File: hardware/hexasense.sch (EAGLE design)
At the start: 15 parts, among them IC1 AT45DB161D-SU

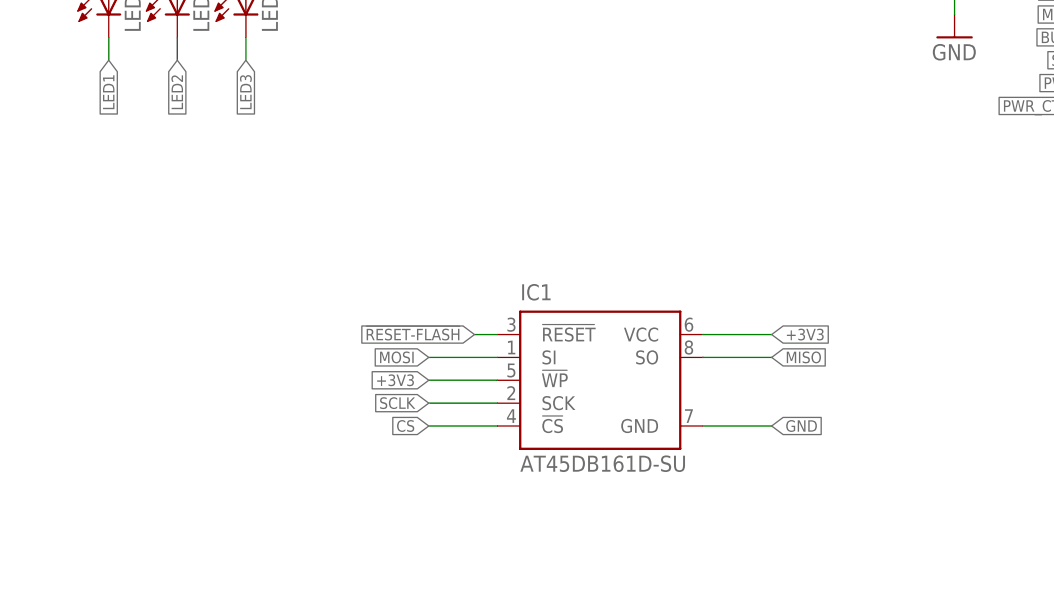
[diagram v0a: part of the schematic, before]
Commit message: added testpads to schematic
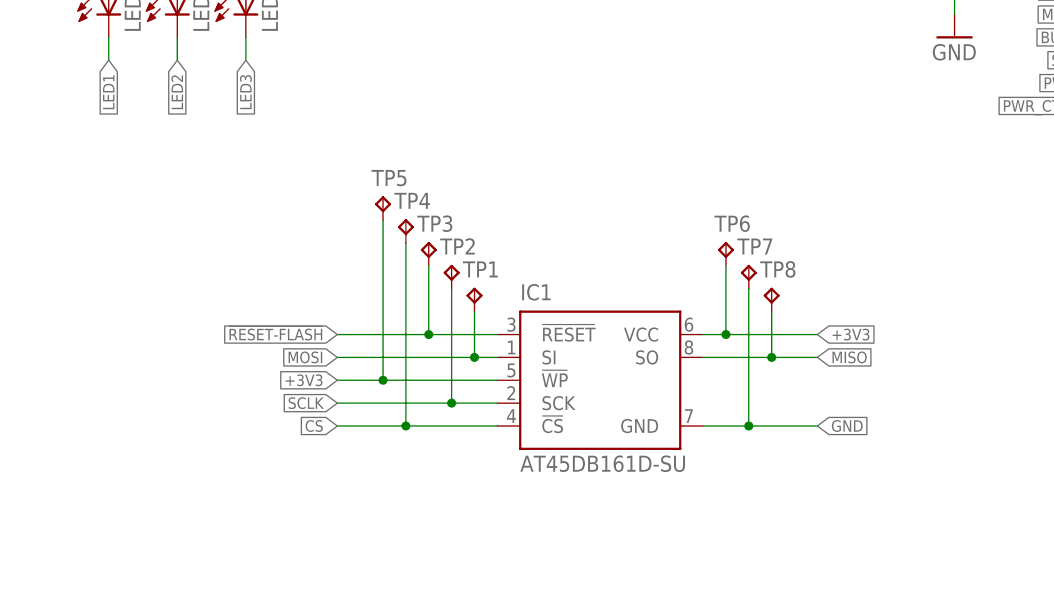
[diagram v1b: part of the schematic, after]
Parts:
- added TP1, TP2, TP3, TP4, TP5, TP6, TP7, TP8: TPB1,27, testpad:TPB1,27
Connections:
- net !RESET-FLASH: now also TP3.TP
- net +3V3: now also TP5.TP, TP6.TP
- net CS: now also TP4.TP
- net GND: now also TP7.TP
- net MISO: now also TP8.TP
- net MOSI: now also TP1.TP
- net SCLK: now also TP2.TP
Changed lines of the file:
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@@
 <part name="+3V6" library="supply1" deviceset="+3V3" device=""/>
 <part name="U$2" library="epaper" deviceset="EPAPER" device=""/>
+<part name="TP1" library="testpad" deviceset="TP" device="B1,27"/>
+<part name="TP2" library="testpad" deviceset="TP" device="B1,27"/>
+<part name="TP3" library="testpad" deviceset="TP" device="B1,27"/>
+<part name="TP4" library="testpad" deviceset="TP" device="B1,27"/>
+<part name="TP5" library="testpad" deviceset="TP" device="B1,27"/>
+<part name="TP6" library="testpad" deviceset="TP" device="B1,27"/>
+<part name="TP7" library="testpad" deviceset="TP" device="B1,27"/>
+<part name="TP8" library="testpad" deviceset="TP" device="B1,27"/>
 </parts>
 <sheets>
@@
 <instance part="+3V6" gate="G$1" x="99.06" y="167.64"/>
 <instance part="U$2" gate="G$1" x="213.36" y="144.78"/>
+<instance part="TP1" gate="G$1" x="124.46" y="114.3"/>
+<instance part="TP2" gate="G$1" x="121.92" y="116.84"/>
+<instance part="TP3" gate="G$1" x="119.38" y="119.38"/>
+<instance part="TP4" gate="G$1" x="116.84" y="121.92"/>
+<instance part="TP5" gate="G$1" x="114.3" y="124.46"/>
+<instance part="TP6" gate="G$1" x="152.4" y="119.38"/>
+<instance part="TP7" gate="G$1" x="154.94" y="116.84"/>
+<instance part="TP8" gate="G$1" x="157.48" y="114.3"/>
 </instances>
 <busses>
@@
 <segment>
 <pinref part="IC1" gate="G$1" pin="GND"/>
-<wire x1="149.86" y1="99.06" x2="157.48" y2="99.06" width="0.1524" layer="91"/>
-<label x="157.48" y="99.06" size="1.27" layer="95" xref="yes"/>
+<wire x1="149.86" y1="99.06" x2="154.94" y2="99.06" width="0.1524" layer="91"/>
+<label x="162.56" y="99.06" size="1.27" layer="95" xref="yes"/>
+<pinref part="TP7" gate="G$1" pin="TP"/>
+<wire x1="154.94" y1="99.06" x2="162.56" y2="99.06" width="0.1524" layer="91"/>
+<wire x1="154.94" y1="114.3" x2="154.94" y2="99.06" width="0.1524" layer="91"/>
+<junction x="154.94" y="99.06"/>
 </segment>
 <segment>
@@
 <segment>
 <pinref part="IC1" gate="G$1" pin="VCC"/>
-<wire x1="149.86" y1="109.22" x2="157.48" y2="109.22" width="0.1524" layer="91"/>
-<label x="157.48" y="109.22" size="1.27" layer="95" xref="yes"/>
+<wire x1="149.86" y1="109.22" x2="152.4" y2="109.22" width="0.1524" layer="91"/>
+<label x="162.56" y="109.22" size="1.27" layer="95" xref="yes"/>
+<pinref part="TP6" gate="G$1" pin="TP"/>
+<wire x1="152.4" y1="109.22" x2="162.56" y2="109.22" width="0.1524" layer="91"/>
+<wire x1="152.4" y1="116.84" x2="152.4" y2="109.22" width="0.1524" layer="91"/>
+<junction x="152.4" y="109.22"/>
 </segment>
 <segment>
 <pinref part="IC1" gate="G$1" pin="!WP"/>
-<wire x1="127" y1="104.14" x2="119.38" y2="104.14" width="0.1524" layer="91"/>
-<label x="119.38" y="104.14" size="1.27" layer="95" rot="R180" xref="yes"/>
+<wire x1="127" y1="104.14" x2="114.3" y2="104.14" width="0.1524" layer="91"/>
+<label x="109.22" y="104.14" size="1.27" layer="95" rot="R180" xref="yes"/>
+<pinref part="TP5" gate="G$1" pin="TP"/>
+<wire x1="114.3" y1="104.14" x2="109.22" y2="104.14" width="0.1524" layer="91"/>
+<wire x1="114.3" y1="121.92" x2="114.3" y2="104.14" width="0.1524" layer="91"/>
+<junction x="114.3" y="104.14"/>
 </segment>
 <segment>
@@
 <pinref part="IC1" gate="G$1" pin="SO"/>
 <wire x1="149.86" y1="106.68" x2="157.48" y2="106.68" width="0.1524" layer="91"/>
-<label x="157.48" y="106.68" size="1.27" layer="95" xref="yes"/>
+<label x="162.56" y="106.68" size="1.27" layer="95" xref="yes"/>
+<pinref part="TP8" gate="G$1" pin="TP"/>
+<wire x1="157.48" y1="106.68" x2="162.56" y2="106.68" width="0.1524" layer="91"/>
+<wire x1="157.48" y1="111.76" x2="157.48" y2="106.68" width="0.1524" layer="91"/>
+<junction x="157.48" y="106.68"/>
 </segment>
 <segment>
@@
 <segment>
 <pinref part="IC1" gate="G$1" pin="SI"/>
-<wire x1="127" y1="106.68" x2="119.38" y2="106.68" width="0.1524" layer="91"/>
-<label x="119.38" y="106.68" size="1.27" layer="95" rot="R180" xref="yes"/>
+<wire x1="127" y1="106.68" x2="124.46" y2="106.68" width="0.1524" layer="91"/>
+<label x="109.22" y="106.68" size="1.27" layer="95" rot="R180" xref="yes"/>
+<pinref part="TP1" gate="G$1" pin="TP"/>
+<wire x1="124.46" y1="106.68" x2="109.22" y2="106.68" width="0.1524" layer="91"/>
+<wire x1="124.46" y1="111.76" x2="124.46" y2="106.68" width="0.1524" layer="91"/>
+<junction x="124.46" y="106.68"/>
 </segment>
 <segment>
@@
 <segment>
 <pinref part="IC1" gate="G$1" pin="!CS"/>
-<wire x1="127" y1="99.06" x2="119.38" y2="99.06" width="0.1524" layer="91"/>
-<label x="119.38" y="99.06" size="1.27" layer="95" rot="R180" xref="yes"/>
+<wire x1="127" y1="99.06" x2="116.84" y2="99.06" width="0.1524" layer="91"/>
+<label x="109.22" y="99.06" size="1.27" layer="95" rot="R180" xref="yes"/>
+<pinref part="TP4" gate="G$1" pin="TP"/>
+<wire x1="116.84" y1="99.06" x2="109.22" y2="99.06" width="0.1524" layer="91"/>
+<wire x1="116.84" y1="119.38" x2="116.84" y2="99.06" width="0.1524" layer="91"/>
+<junction x="116.84" y="99.06"/>
 </segment>
 <segment>
@@
 <segment>
 <pinref part="IC1" gate="G$1" pin="!RESET"/>
-<wire x1="127" y1="109.22" x2="124.46" y2="109.22" width="0.1524" layer="91"/>
-<label x="124.46" y="109.22" size="1.27" layer="95" rot="R180" xref="yes"/>
+<wire x1="127" y1="109.22" x2="119.38" y2="109.22" width="0.1524" layer="91"/>
+<label x="109.22" y="109.22" size="1.27" layer="95" rot="R180" xref="yes"/>
+<pinref part="TP3" gate="G$1" pin="TP"/>
+<wire x1="119.38" y1="109.22" x2="109.22" y2="109.22" width="0.1524" layer="91"/>
+<wire x1="119.38" y1="116.84" x2="119.38" y2="109.22" width="0.1524" layer="91"/>
+<junction x="119.38" y="109.22"/>
 </segment>
 <segment>
@@
 <segment>
 <pinref part="IC1" gate="G$1" pin="SCK"/>
-<wire x1="127" y1="101.6" x2="119.38" y2="101.6" width="0.1524" layer="91"/>
-<label x="119.38" y="101.6" size="1.27" layer="95" rot="R180" xref="yes"/>
-</segment>
-</net>
+<wire x1="127" y1="101.6" x2="121.92" y2="101.6" width="0.1524" layer="91"/>
+<label x="109.22" y="101.6" size="1.27" layer="95" rot="R180" xref="yes"/>
+<pinref part="TP2" gate="G$1" pin="TP"/>
+<wire x1="121.92" y1="101.6" x2="109.22" y2="101.6" width="0.1524" layer="91"/>
+<wire x1="121.92" y1="114.3" x2="121.92" y2="101.6" width="0.1524" layer="91"/>
+<junction x="121.92" y="101.6"/>
+</segment>
+</net>

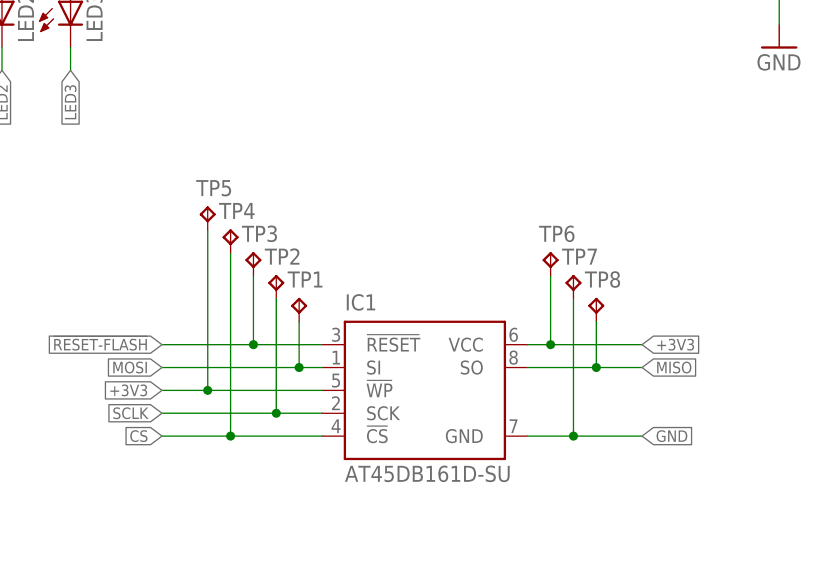
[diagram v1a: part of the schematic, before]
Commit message: testpads and placement print
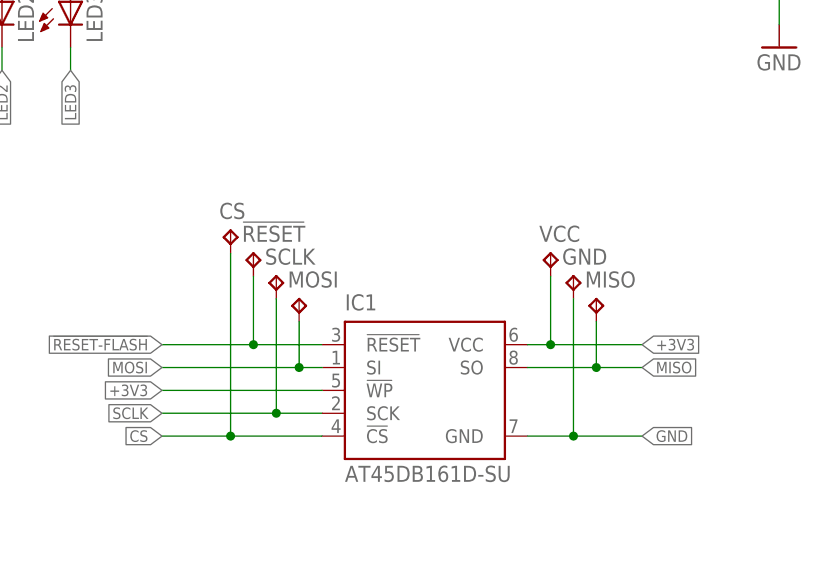
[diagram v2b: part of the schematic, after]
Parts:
- removed TP5: TPB1,27, testpad:TPB1,27
- renumbered TP1 to MOSI, TP2 to SCLK, TP3 to !RESET, TP4 to CS, TP6 to VCC, TP7 to GND, TP8 to MISO
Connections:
- net +3V3: no longer TP5.TP
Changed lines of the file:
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@@
 <part name="+3V6" library="supply1" deviceset="+3V3" device=""/>
 <part name="U$2" library="epaper" deviceset="EPAPER" device=""/>
-<part name="TP1" library="testpad" deviceset="TP" device="B1,27"/>
-<part name="TP2" library="testpad" deviceset="TP" device="B1,27"/>
-<part name="TP3" library="testpad" deviceset="TP" device="B1,27"/>
-<part name="TP4" library="testpad" deviceset="TP" device="B1,27"/>
-<part name="TP5" library="testpad" deviceset="TP" device="B1,27"/>
-<part name="TP6" library="testpad" deviceset="TP" device="B1,27"/>
-<part name="TP7" library="testpad" deviceset="TP" device="B1,27"/>
-<part name="TP8" library="testpad" deviceset="TP" device="B1,27"/>
+<part name="MOSI" library="testpad" deviceset="TP" device="B1,27"/>
+<part name="SCLK" library="testpad" deviceset="TP" device="B1,27"/>
+<part name="!RESET" library="testpad" deviceset="TP" device="B1,27"/>
+<part name="CS" library="testpad" deviceset="TP" device="B1,27"/>
+<part name="VCC" library="testpad" deviceset="TP" device="B1,27"/>
+<part name="GND" library="testpad" deviceset="TP" device="B1,27"/>
+<part name="MISO" library="testpad" deviceset="TP" device="B1,27"/>
 </parts>
 <sheets>
@@
 <instance part="+3V6" gate="G$1" x="99.06" y="167.64"/>
 <instance part="U$2" gate="G$1" x="213.36" y="144.78"/>
-<instance part="TP1" gate="G$1" x="124.46" y="114.3"/>
-<instance part="TP2" gate="G$1" x="121.92" y="116.84"/>
-<instance part="TP3" gate="G$1" x="119.38" y="119.38"/>
-<instance part="TP4" gate="G$1" x="116.84" y="121.92"/>
-<instance part="TP5" gate="G$1" x="114.3" y="124.46"/>
-<instance part="TP6" gate="G$1" x="152.4" y="119.38"/>
-<instance part="TP7" gate="G$1" x="154.94" y="116.84"/>
-<instance part="TP8" gate="G$1" x="157.48" y="114.3"/>
+<instance part="MOSI" gate="G$1" x="124.46" y="114.3"/>
+<instance part="SCLK" gate="G$1" x="121.92" y="116.84"/>
+<instance part="!RESET" gate="G$1" x="119.38" y="119.38"/>
+<instance part="CS" gate="G$1" x="116.84" y="121.92"/>
+<instance part="VCC" gate="G$1" x="152.4" y="119.38"/>
+<instance part="GND" gate="G$1" x="154.94" y="116.84"/>
+<instance part="MISO" gate="G$1" x="157.48" y="114.3"/>
 </instances>
 <busses>
@@
 <wire x1="149.86" y1="99.06" x2="154.94" y2="99.06" width="0.1524" layer="91"/>
 <label x="162.56" y="99.06" size="1.27" layer="95" xref="yes"/>
-<pinref part="TP7" gate="G$1" pin="TP"/>
+<pinref part="GND" gate="G$1" pin="TP"/>
 <wire x1="154.94" y1="99.06" x2="162.56" y2="99.06" width="0.1524" layer="91"/>
 <wire x1="154.94" y1="114.3" x2="154.94" y2="99.06" width="0.1524" layer="91"/>
@@
 <wire x1="149.86" y1="109.22" x2="152.4" y2="109.22" width="0.1524" layer="91"/>
 <label x="162.56" y="109.22" size="1.27" layer="95" xref="yes"/>
-<pinref part="TP6" gate="G$1" pin="TP"/>
+<pinref part="VCC" gate="G$1" pin="TP"/>
 <wire x1="152.4" y1="109.22" x2="162.56" y2="109.22" width="0.1524" layer="91"/>
 <wire x1="152.4" y1="116.84" x2="152.4" y2="109.22" width="0.1524" layer="91"/>
@@
 <segment>
 <pinref part="IC1" gate="G$1" pin="!WP"/>
-<wire x1="127" y1="104.14" x2="114.3" y2="104.14" width="0.1524" layer="91"/>
+<wire x1="127" y1="104.14" x2="109.22" y2="104.14" width="0.1524" layer="91"/>
 <label x="109.22" y="104.14" size="1.27" layer="95" rot="R180" xref="yes"/>
-<pinref part="TP5" gate="G$1" pin="TP"/>
-<wire x1="114.3" y1="104.14" x2="109.22" y2="104.14" width="0.1524" layer="91"/>
-<wire x1="114.3" y1="121.92" x2="114.3" y2="104.14" width="0.1524" layer="91"/>
-<junction x="114.3" y="104.14"/>
 </segment>
 <segment>
@@
 <wire x1="149.86" y1="106.68" x2="157.48" y2="106.68" width="0.1524" layer="91"/>
 <label x="162.56" y="106.68" size="1.27" layer="95" xref="yes"/>
-<pinref part="TP8" gate="G$1" pin="TP"/>
+<pinref part="MISO" gate="G$1" pin="TP"/>
 <wire x1="157.48" y1="106.68" x2="162.56" y2="106.68" width="0.1524" layer="91"/>
 <wire x1="157.48" y1="111.76" x2="157.48" y2="106.68" width="0.1524" layer="91"/>
@@
 <wire x1="127" y1="106.68" x2="124.46" y2="106.68" width="0.1524" layer="91"/>
 <label x="109.22" y="106.68" size="1.27" layer="95" rot="R180" xref="yes"/>
-<pinref part="TP1" gate="G$1" pin="TP"/>
+<pinref part="MOSI" gate="G$1" pin="TP"/>
 <wire x1="124.46" y1="106.68" x2="109.22" y2="106.68" width="0.1524" layer="91"/>
 <wire x1="124.46" y1="111.76" x2="124.46" y2="106.68" width="0.1524" layer="91"/>
@@
 <wire x1="127" y1="99.06" x2="116.84" y2="99.06" width="0.1524" layer="91"/>
 <label x="109.22" y="99.06" size="1.27" layer="95" rot="R180" xref="yes"/>
-<pinref part="TP4" gate="G$1" pin="TP"/>
+<pinref part="CS" gate="G$1" pin="TP"/>
 <wire x1="116.84" y1="99.06" x2="109.22" y2="99.06" width="0.1524" layer="91"/>
 <wire x1="116.84" y1="119.38" x2="116.84" y2="99.06" width="0.1524" layer="91"/>
@@
 <wire x1="127" y1="109.22" x2="119.38" y2="109.22" width="0.1524" layer="91"/>
 <label x="109.22" y="109.22" size="1.27" layer="95" rot="R180" xref="yes"/>
-<pinref part="TP3" gate="G$1" pin="TP"/>
+<pinref part="!RESET" gate="G$1" pin="TP"/>
 <wire x1="119.38" y1="109.22" x2="109.22" y2="109.22" width="0.1524" layer="91"/>
 <wire x1="119.38" y1="116.84" x2="119.38" y2="109.22" width="0.1524" layer="91"/>
@@
 <wire x1="127" y1="101.6" x2="121.92" y2="101.6" width="0.1524" layer="91"/>
 <label x="109.22" y="101.6" size="1.27" layer="95" rot="R180" xref="yes"/>
-<pinref part="TP2" gate="G$1" pin="TP"/>
+<pinref part="SCLK" gate="G$1" pin="TP"/>
 <wire x1="121.92" y1="101.6" x2="109.22" y2="101.6" width="0.1524" layer="91"/>
 <wire x1="121.92" y1="114.3" x2="121.92" y2="101.6" width="0.1524" layer="91"/>

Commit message: several minor changes
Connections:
- removed net DATA: U$4.PD3
- removed net N$8: U$4.PB2
- net BUSY: now also U$4.PD3
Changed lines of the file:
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@@
-</segment>
-</net>
-<net name="DATA" class="0">
-<segment>
-<wire x1="53.34" y1="15.24" x2="60.96" y2="15.24" width="0.1524" layer="91"/>
-<label x="60.96" y="15.24" size="1.27" layer="95" xref="yes"/>
-<pinref part="U$4" gate="G$1" pin="PD3"/>
 </segment>
 </net>
@@
 <label x="193.04" y="142.24" size="1.27" layer="95" rot="R180" xref="yes"/>
 </segment>
+<segment>
+<pinref part="U$4" gate="G$1" pin="PD3"/>
+<wire x1="53.34" y1="15.24" x2="60.96" y2="15.24" width="0.1524" layer="91"/>
+<label x="60.96" y="15.24" size="1.27" layer="95" xref="yes"/>
+</segment>
 </net>
 <net name="PWM" class="0">
@@
 </segment>
 </net>
-<net name="N$8" class="0">
-<segment>
-<pinref part="U$4" gate="G$1" pin="PB2"/>
-<wire x1="27.94" y1="17.78" x2="20.32" y2="17.78" width="0.1524" layer="91"/>
-<label x="20.32" y="17.78" size="1.27" layer="95" rot="R180" xref="yes"/>
-</segment>
-</net>
